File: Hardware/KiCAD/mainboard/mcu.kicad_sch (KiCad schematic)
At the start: 12 parts, among them U1 STM32F427ZGTx, Y1 32 kHz, Y2 8 MHz

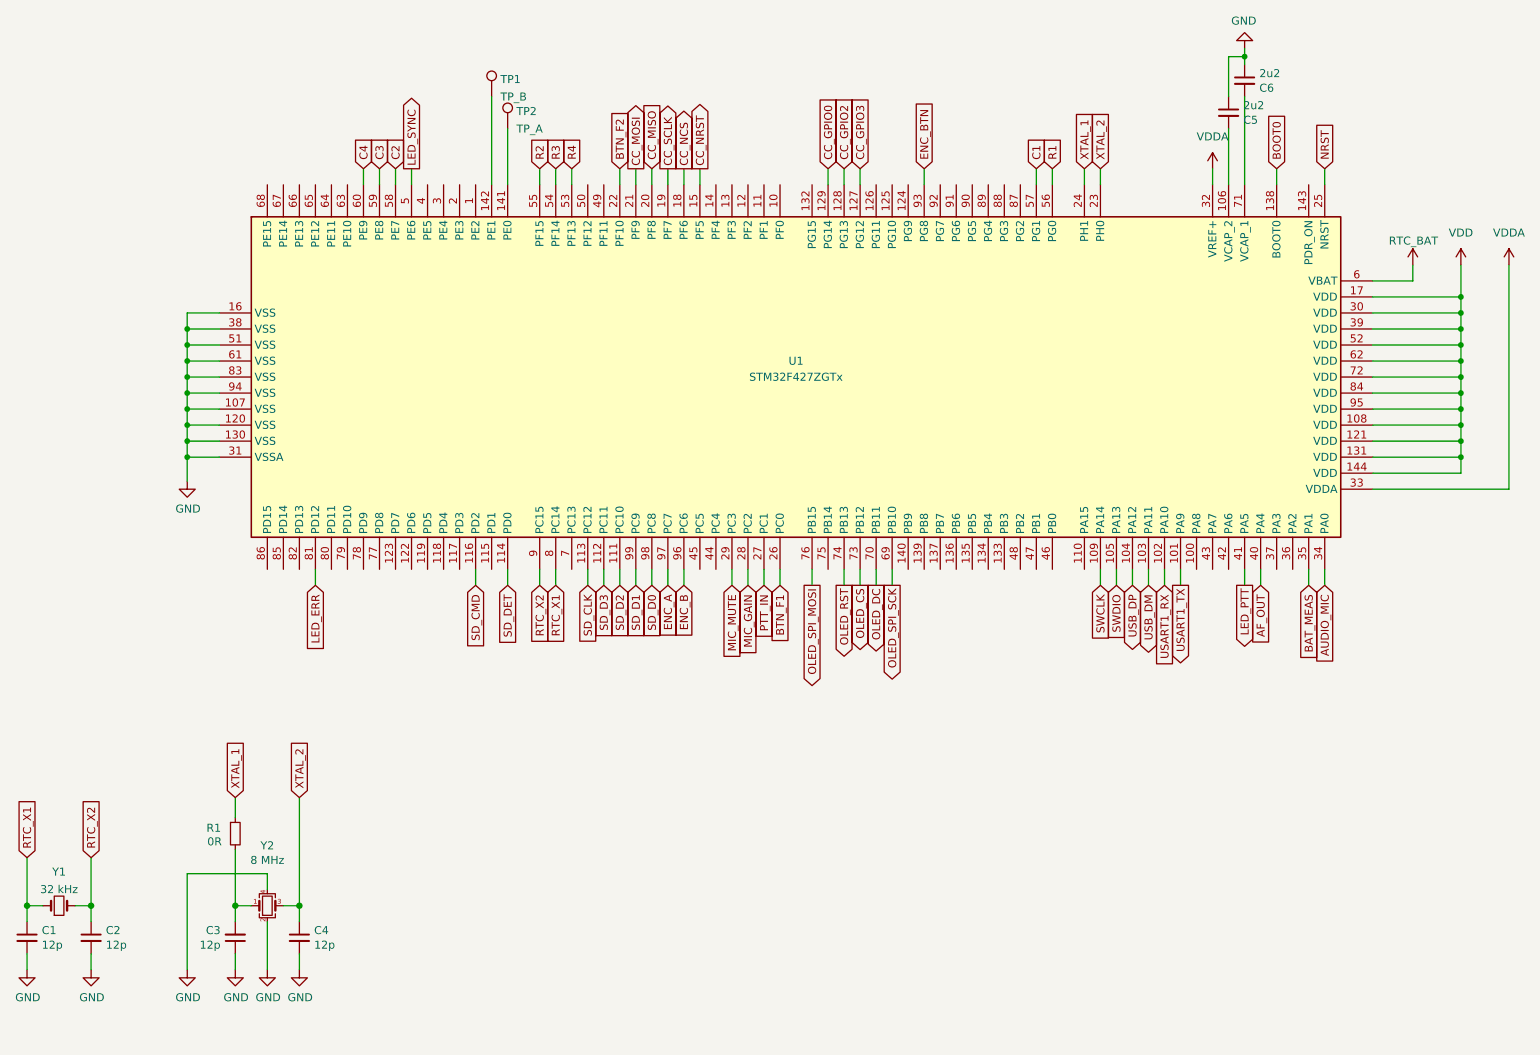
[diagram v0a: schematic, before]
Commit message: J3 UART conn change
Fixes #33
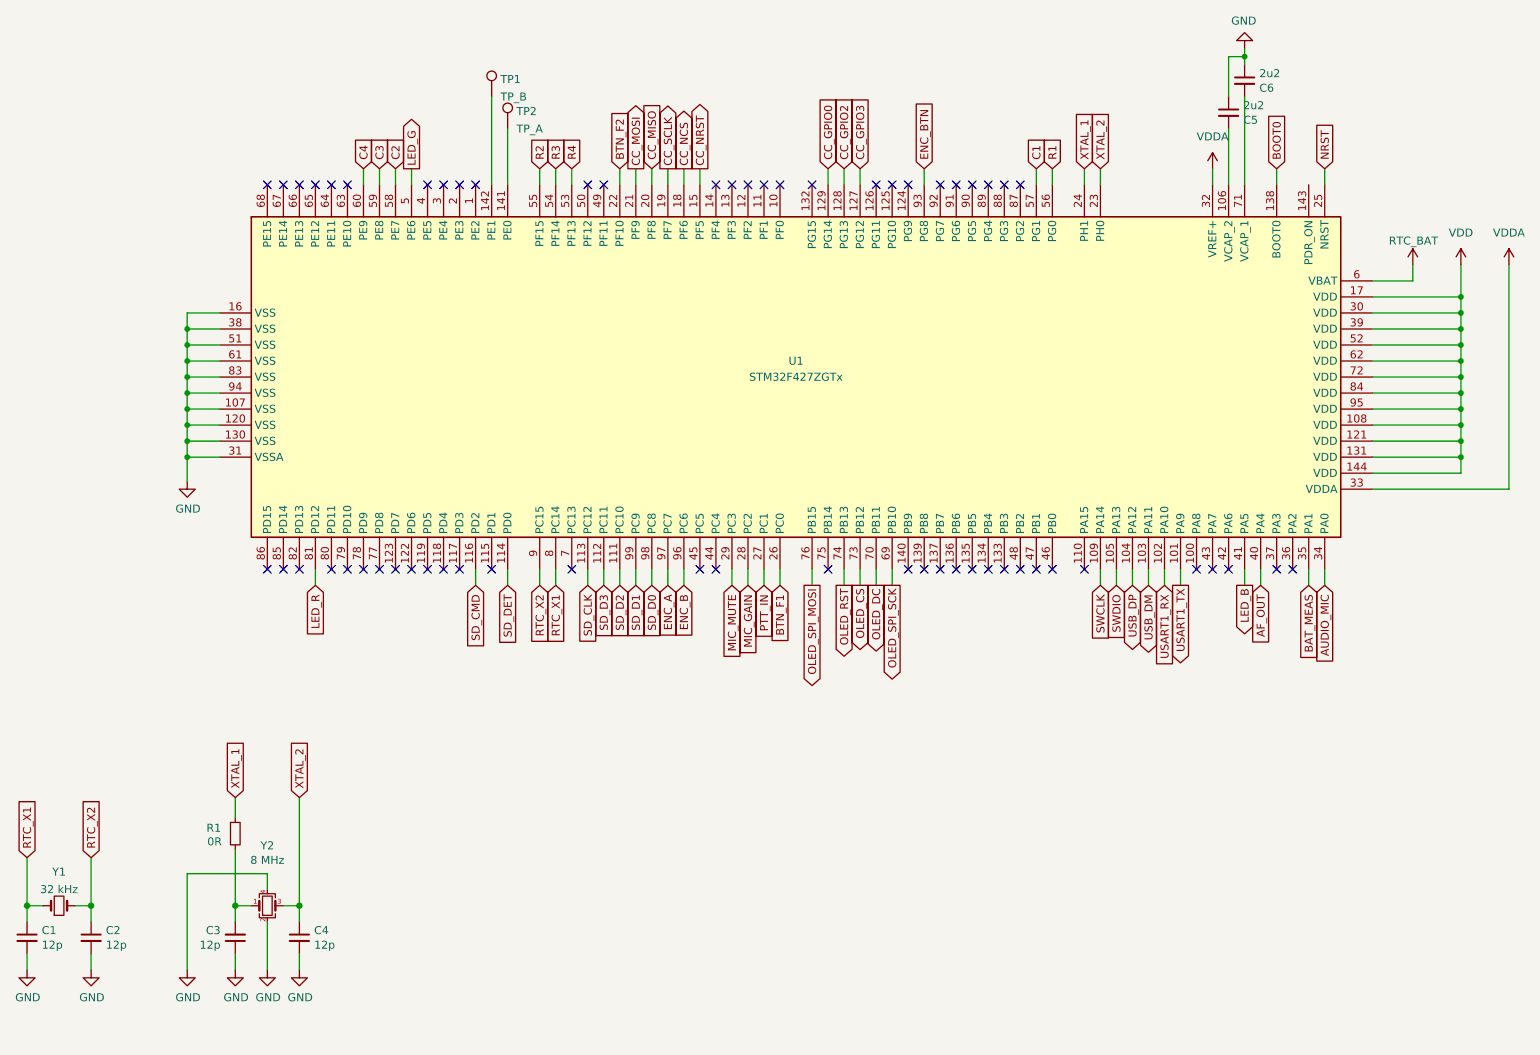
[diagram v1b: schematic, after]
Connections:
- net LED_ERR renamed LED_R
- net LED_PTT renamed LED_B
- net LED_SYNC renamed LED_G
- no-connect marks 0 -> 60
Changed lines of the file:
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@@
   (junction (at 255.27 91.44) (diameter 0) (color 0 0 0 0)
   )
+  (no_connect (at 134.62 114.3))
+  (no_connect (at 137.16 114.3))
+  (no_connect (at 154.94 114.3))
+  (no_connect (at 167.64 114.3))
+  (no_connect (at 170.18 114.3))
+  (no_connect (at 172.72 114.3))
+  (no_connect (at 175.26 114.3))
+  (no_connect (at 177.8 114.3))
+  (no_connect (at 180.34 114.3))
+  (no_connect (at 228.6 114.3))
+  (no_connect (at 226.06 114.3))
+  (no_connect (at 182.88 114.3))
+  (no_connect (at 185.42 114.3))
+  (no_connect (at 187.96 114.3))
+  (no_connect (at 190.5 114.3))
+  (no_connect (at 195.58 114.3))
+  (no_connect (at 213.36 114.3))
+  (no_connect (at 218.44 114.3))
+  (no_connect (at 215.9 114.3))
+  (no_connect (at 81.28 114.3))
+  (no_connect (at 78.74 114.3))
+  (no_connect (at 76.2 114.3))
+  (no_connect (at 71.12 114.3))
+  (no_connect (at 66.04 114.3))
+  (no_connect (at 68.58 114.3))
+  (no_connect (at 96.52 114.3))
+  (no_connect (at 101.6 114.3))
+  (no_connect (at 93.98 114.3))
+  (no_connect (at 114.3 114.3))
+  (no_connect (at 91.44 114.3))
+  (no_connect (at 88.9 114.3))
+  (no_connect (at 86.36 114.3))
+  (no_connect (at 83.82 114.3))
+  (no_connect (at 78.74 53.34))
+  (no_connect (at 76.2 53.34))
+  (no_connect (at 73.66 53.34))
+  (no_connect (at 71.12 53.34))
+  (no_connect (at 68.58 53.34))
+  (no_connect (at 66.04 53.34))
+  (no_connect (at 91.44 53.34))
+  (no_connect (at 119.38 53.34))
+  (no_connect (at 116.84 53.34))
+  (no_connect (at 99.06 53.34))
+  (no_connect (at 93.98 53.34))
+  (no_connect (at 96.52 53.34))
+  (no_connect (at 162.56 53.34))
+  (no_connect (at 165.1 53.34))
+  (no_connect (at 167.64 53.34))
+  (no_connect (at 152.4 53.34))
+  (no_connect (at 139.7 53.34))
+  (no_connect (at 147.32 53.34))
+  (no_connect (at 144.78 53.34))
+  (no_connect (at 142.24 53.34))
+  (no_connect (at 137.16 53.34))
+  (no_connect (at 180.34 53.34))
+  (no_connect (at 182.88 53.34))
+  (no_connect (at 172.72 53.34))
+  (no_connect (at 175.26 53.34))
+  (no_connect (at 177.8 53.34))
+  (no_connect (at 185.42 53.34))
   (wire (pts (xy 53.34 100.33) (xy 53.34 96.52))
     (stroke (width 0) (type default) (color 0 0 0 0))
@@
     )
   )
-  (global_label "LED_SYNC" (shape output) (at 88.9 50.8 90) (fields_autoplaced)
-    (effects (font (size 1.27 1.27)) (justify left))
-    (property "Intersheet References" "${INTERSHEET_REFS}" (id 0) (at 88.8206 39.0736 90)
+  (global_label "LED_G" (shape output) (at 88.9 50.8 90) (fields_autoplaced)
+    (effects (font (size 1.27 1.27)) (justify left))
+    (property "Intersheet References" "${INTERSHEET_REFS}" (id 0) (at 88.8206 42.7021 90)
       (effects (font (size 1.27 1.27)) (justify left) hide)
     )
@@
     )
   )
-  (global_label "LED_ERR" (shape input) (at 73.66 116.84 270) (fields_autoplaced)
-    (effects (font (size 1.27 1.27)) (justify right))
-    (property "Intersheet References" "${INTERSHEET_REFS}" (id 0) (at 73.5806 127.3569 90)
+  (global_label "LED_R" (shape input) (at 73.66 116.84 270) (fields_autoplaced)
+    (effects (font (size 1.27 1.27)) (justify right))
+    (property "Intersheet References" "${INTERSHEET_REFS}" (id 0) (at 73.5806 124.9379 90)
       (effects (font (size 1.27 1.27)) (justify right) hide)
     )
@@
     )
   )
-  (global_label "LED_PTT" (shape output) (at 220.98 116.84 270) (fields_autoplaced)
-    (effects (font (size 1.27 1.27)) (justify right))
-    (property "Intersheet References" "${INTERSHEET_REFS}" (id 0) (at 220.9006 126.8731 90)
-      (effects (font (size 1.27 1.27)) (justify right) hide)
-    )
+  (global_label "LED_B" (shape output) (at 220.98 116.84 270) (fields_autoplaced)
+    (effects (font (size 1.27 1.27)) (justify right))
+    (property "Intersheet References" "${INTERSHEET_REFS}" (id 0) (at 220.9006 124.9379 90)
+      (effects (font (size 1.27 1.27)) (justify right) hide)
+    )

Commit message: MCU swap
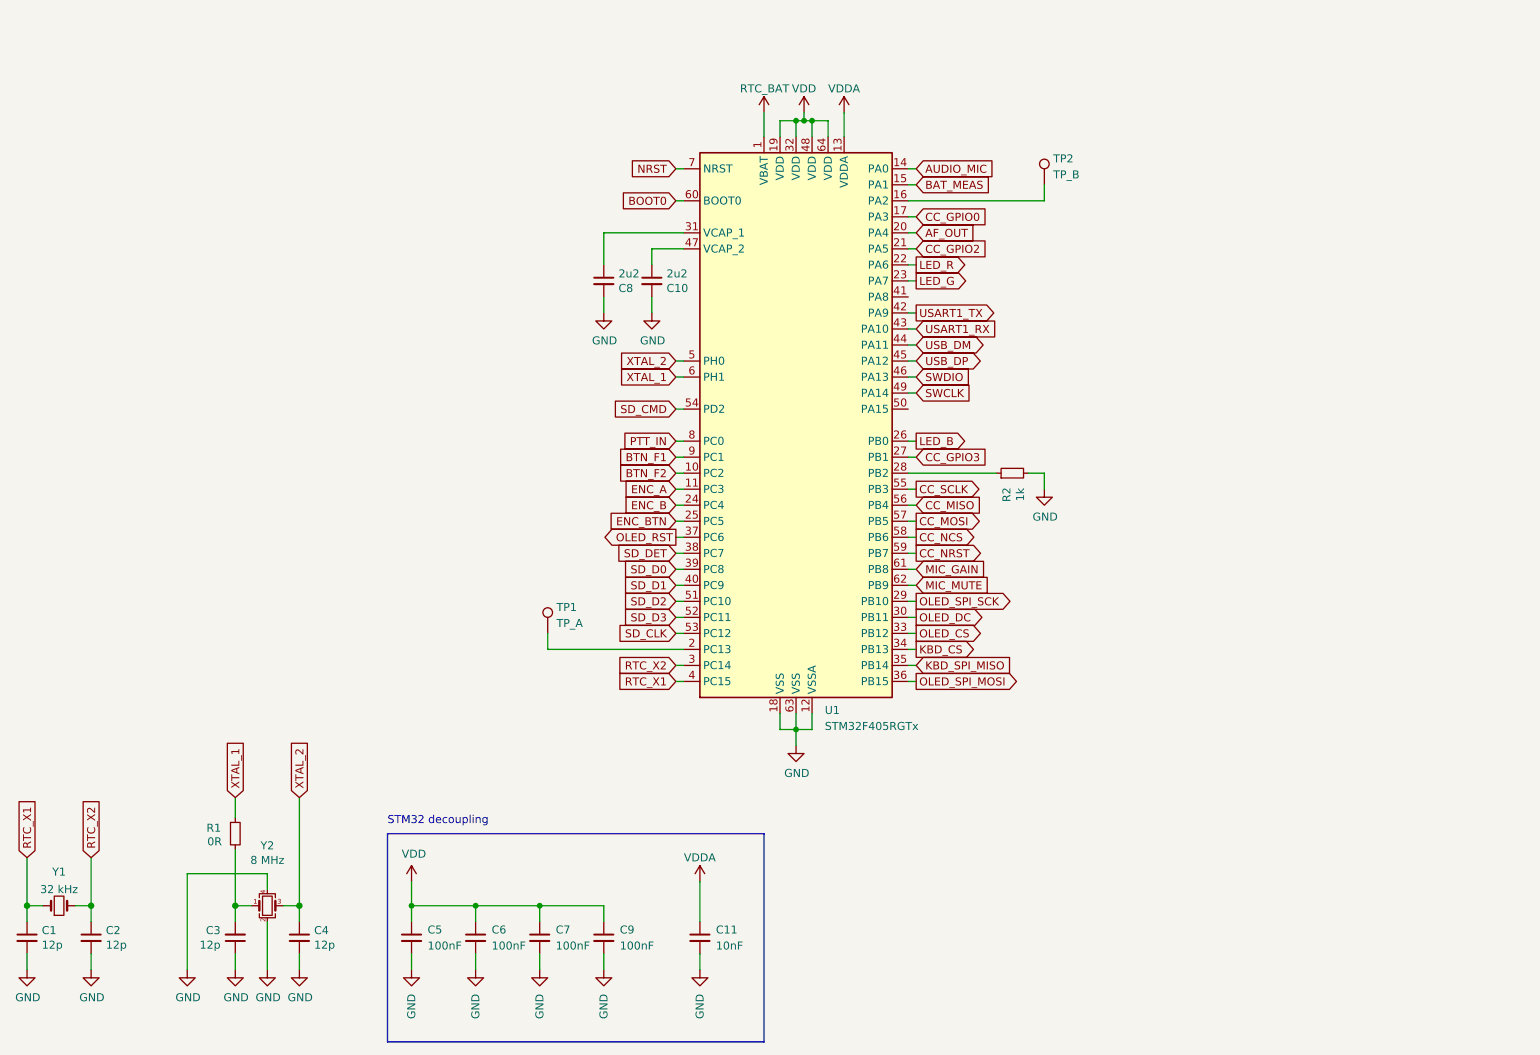
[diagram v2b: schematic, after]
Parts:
- removed U1: STM32F427ZGTx, Package_QFP:LQFP-144_20x20mm_P0.5mm, symbol MCU_ST_STM32F4:STM32F427ZGTx
- added C11: 10nF, Capacitor_SMD:C_0402_1005Metric, symbol Device:C_Small
- added C5, C6, C7, C9: 100nF, Capacitor_SMD:C_0402_1005Metric, symbol Device:C_Small
- added R2: 1k, Resistor_SMD:R_0402_1005Metric, symbol Device:R_Small
- added U1: STM32F405RGTx, Package_QFP:LQFP-64_10x10mm_P0.5mm, symbol MCU_ST_STM32F4:STM32F405RGTx
- TP1: value TP_B -> TP_A
- TP2: value TP_A -> TP_B
- renumbered C5 to C10, C6 to C8
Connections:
- net AF_OUT: now also U1.20 (PA4)
- net AUDIO_MIC: now also U1.14 (PA0)
- net BAT_MEAS: now also U1.15 (PA1)
- net BOOT0: now also U1.60 (BOOT0)
- net BTN_F1: now also U1.9 (PC1)
- net BTN_F2: now also U1.10 (PC2)
- net CC_GPIO0: now also U1.17 (PA3)
- net CC_GPIO2: now also U1.21 (PA5)
- net CC_GPIO3: now also U1.27 (PB1)
- net CC_MISO: now also U1.56 (PB4)
- net CC_MOSI: now also U1.57 (PB5)
- net CC_NCS: now also U1.58 (PB6)
- net CC_NRST: now also U1.59 (PB7)
- net CC_SCLK: now also U1.55 (PB3)
- net ENC_A: now also U1.11 (PC3)
- net ENC_B: now also U1.24 (PC4)
- net ENC_BTN: now also U1.25 (PC5)
- net GND: now also C10.2, C8.2, C11.2, C5.2, C6.2, C7.2, C9.2, R2.2, U1.12 (VSSA), U1.18 (VSS), U1.63 (VSS); no longer C10.1, C8.1
- net LED_B: now also U1.26 (PB0)
- net LED_G: now also U1.23 (PA7)
- net LED_R: now also U1.22 (PA6)
- net MIC_GAIN: now also U1.61 (PB8)
- net MIC_MUTE: now also U1.62 (PB9)
- net NRST: now also U1.7 (NRST)
- net OLED_CS: now also U1.33 (PB12)
- net OLED_DC: now also U1.30 (PB11)
- net OLED_RST: now also U1.37 (PC6)
- net OLED_SPI_MOSI: now also U1.36 (PB15)
- net OLED_SPI_SCK: now also U1.29 (PB10)
- net PTT_IN: now also U1.8 (PC0)
- net RTC_X1: now also U1.4 (PC15)
- net RTC_X2: now also U1.3 (PC14)
- net SD_CLK: now also U1.53 (PC12)
- net SD_CMD: now also U1.54 (PD2)
- net SD_D0: now also U1.39 (PC8)
- net SD_D1: now also U1.40 (PC9)
- net SD_D2: now also U1.51 (PC10)
- net SD_D3: now also U1.52 (PC11)
- net SD_DET: now also U1.38 (PC7)
- net SWCLK: now also U1.49 (PA14)
- net SWDIO: now also U1.46 (PA13)
- net USART1_RX: now also U1.43 (PA10)
- net USART1_TX: now also U1.42 (PA9)
- net USB_DM: now also U1.44 (PA11)
- net USB_DP: now also U1.45 (PA12)
- net VBAT: now also U1.1 (VBAT)
- net VDD: now also C5.1, C6.1, C7.1, C9.1, U1.19 (VDD), U1.32 (VDD), U1.48 (VDD), U1.64 (VDD)
- net VDDA: now also C11.1, U1.13 (VDDA)
- net XTAL_1: now also U1.6 (PH1)
- net XTAL_2: now also U1.5 (PH0)
- net at TP1.1: now also U1.2 (PC13)
- net at TP2.1: now also U1.16 (PA2)
- new net: R2.1, U1.28 (PB2)
- new net: C10.1, U1.47 (VCAP_2)
- new net: C8.1, U1.31 (VCAP_1)
- new net KBD_CS: U1.34 (PB13)
- new net KBD_SPI_MISO: U1.35 (PB14)
- no-connect marks 60 -> 0
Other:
- note added: "STM32 decoupling"
- moved on the sheet: C10, C8, TP1, TP2

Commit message: Removed RTC
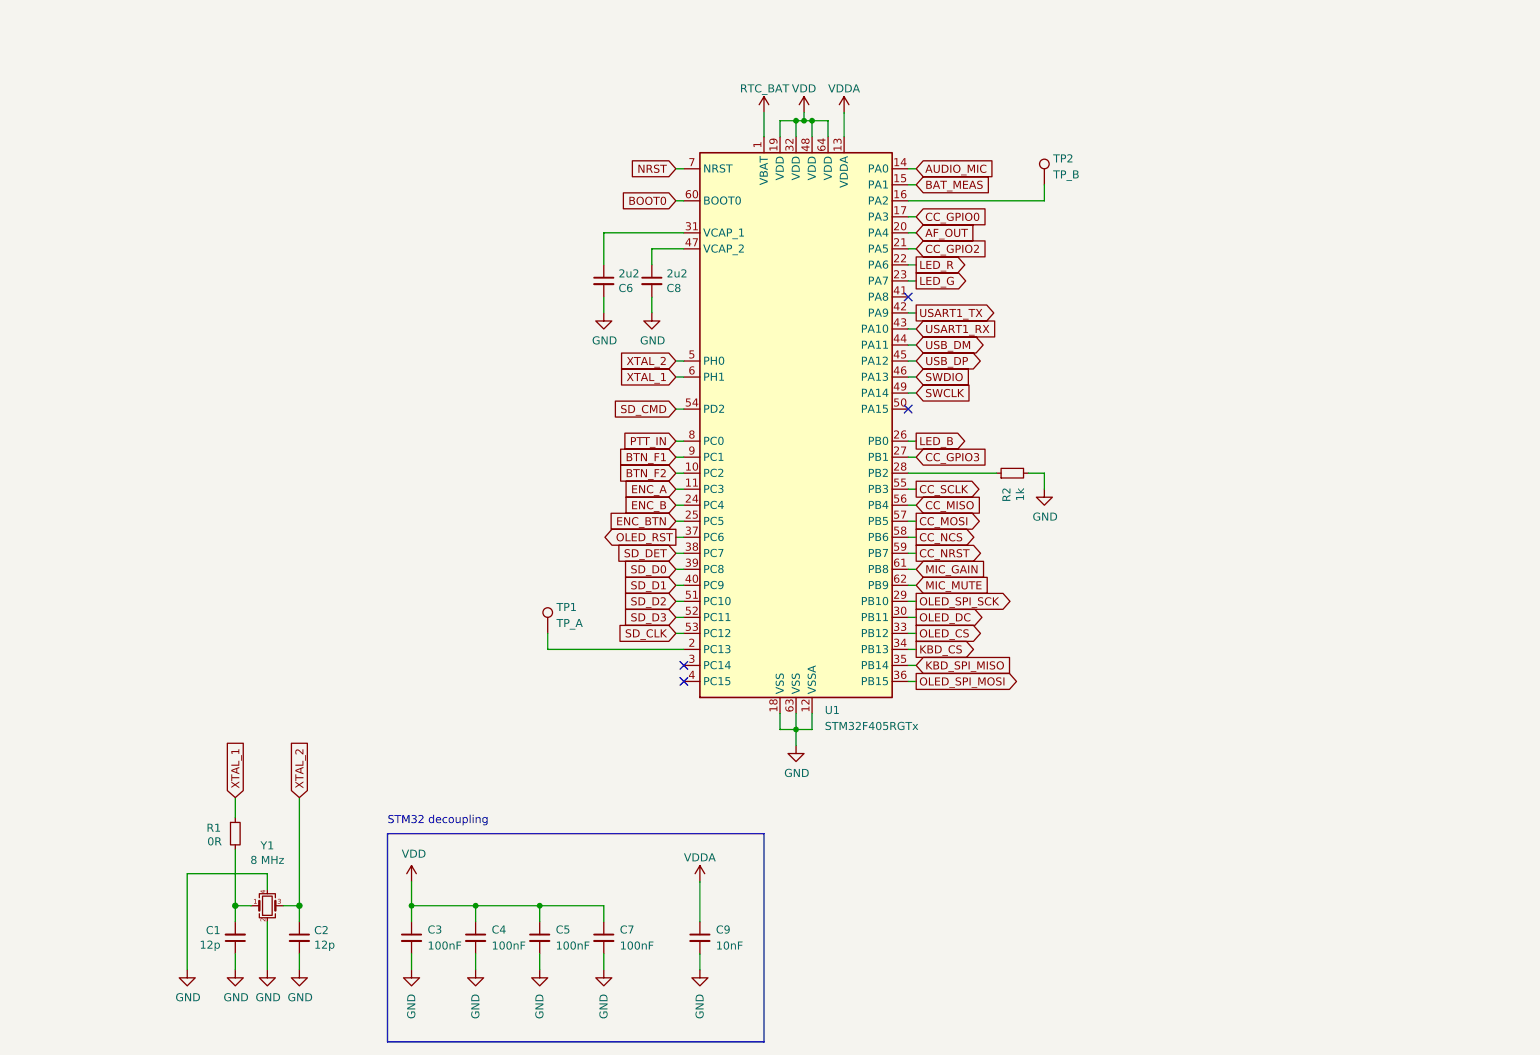
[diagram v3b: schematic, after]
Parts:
- removed C1, C2: 12p, pkl_dipol:C_0603, symbol pkl_device:pkl_C_Small
- removed Y1: 32 kHz, Crystal:Crystal_SMD_MicroCrystal_CC8V-T1A-2Pin_2.0x1.2mm, symbol Device:Crystal_Small
- renumbered C3 to C1, C4 to C2, C5 to C3, C6 to C4, C7 to C5, C8 to C6, C9 to C7, C10 to C8, C11 to C9, Y2 to Y1
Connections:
- net RTC_X1: no longer names the net of U1.4 (PC15)
- net RTC_X2: no longer names the net of U1.3 (PC14)
- no-connect marks 0 -> 4
